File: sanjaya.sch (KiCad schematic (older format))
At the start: 10 parts, among them J1 PWR_SUPPLY, J15 Serial, J2 Digital_Input_Signals, J3 Digital_Gnd, J4 Screw_Terminal_01x03, J5 Screw_Terminal_01x03, J6 Screw_Terminal_01x02, J7 Screw_Terminal_01x02, U2 MCP9700T-ETT

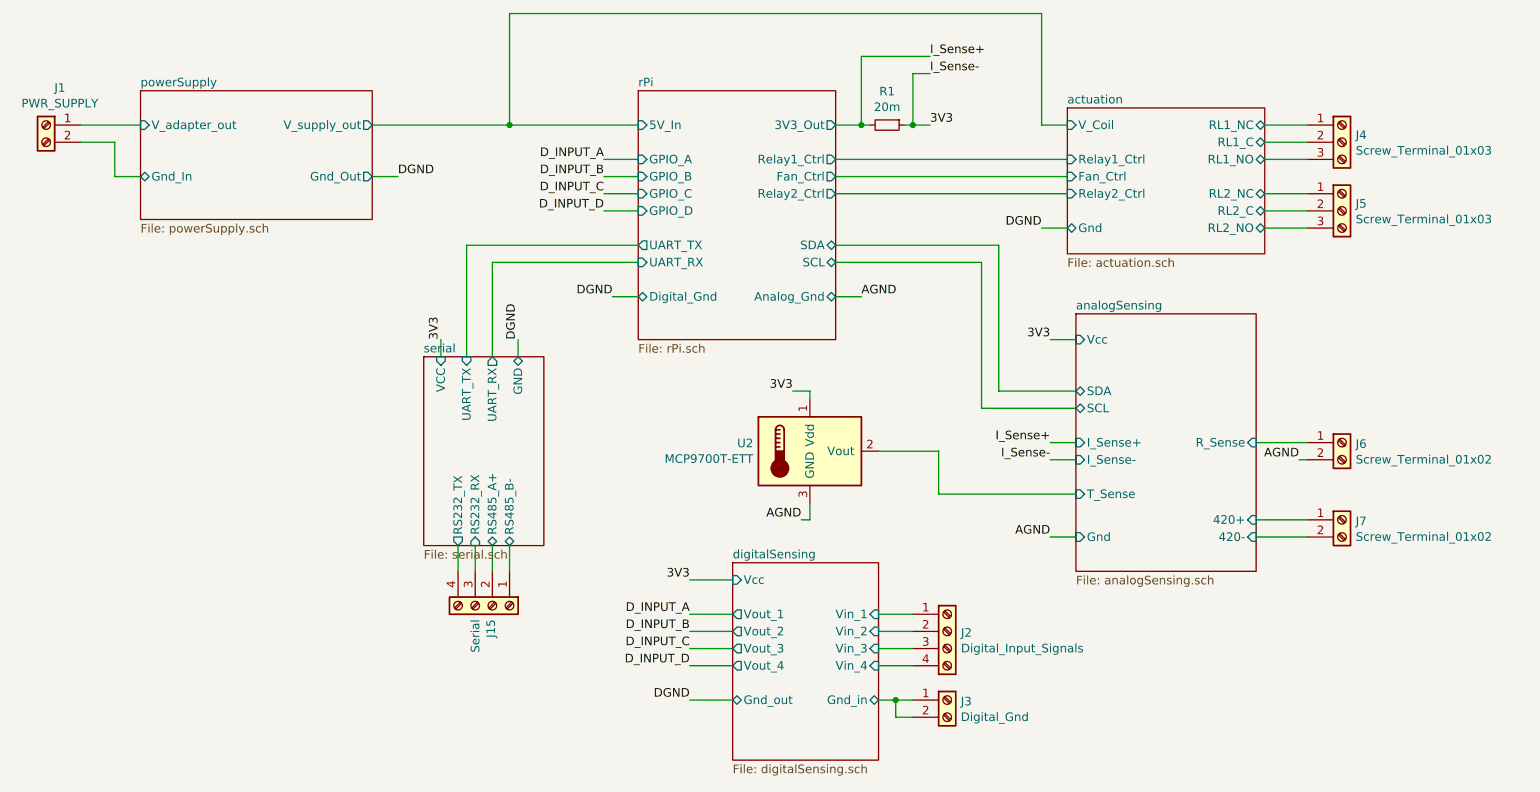
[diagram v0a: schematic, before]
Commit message: Changes: 1. Some net names, connector names changed to be more meaningful 2. I2C connector added 3. Mistake in power bank bypass connection rectified 4. Layout changed. Almost finalized.
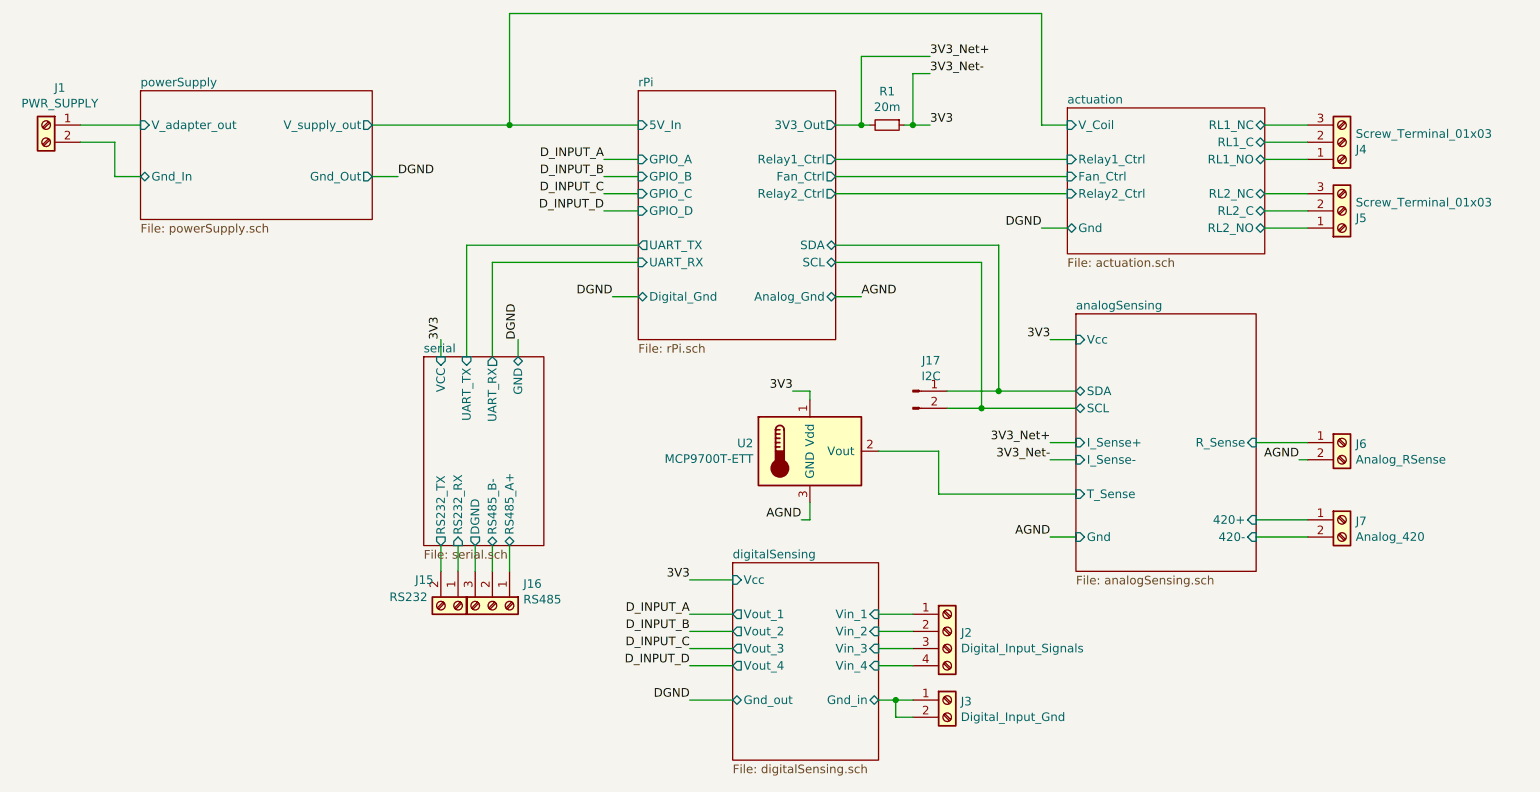
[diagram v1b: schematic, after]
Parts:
- removed J15: Serial, TerminalBlock_Phoenix:TerminalBlock_Phoenix_MKDS-1,5-4-5.08_1x04_P5.08mm_Horizontal, symbol Connector:Screw_Terminal_01x04
- added J15: RS232, TerminalBlock_Phoenix:TerminalBlock_Phoenix_MKDS-1,5-2-5.08_1x02_P5.08mm_Horizontal, symbol Connector:Screw_Terminal_01x02
- added J16: RS485, TerminalBlock_Phoenix:TerminalBlock_Phoenix_MKDS-1,5-3-5.08_1x03_P5.08mm_Horizontal, symbol Connector:Screw_Terminal_01x03
- added J17: I2C, Connector_JST:JST_EH_B02B-EH-A_1x02_P2.50mm_Vertical, symbol Connector:Conn_01x02_Male
- J3: value Digital_Gnd -> Digital_Input_Gnd
- J6: value Screw_Terminal_01x02 -> Analog_RSense
- J7: value Screw_Terminal_01x02 -> Analog_420
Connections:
- net actuation/RL1_NC: now also J4.3 (Pin_3); no longer J4.1 (Pin_1)
- net actuation/RL1_NO: now also J4.1 (Pin_1); no longer J4.3 (Pin_3)
- net actuation/RL2_NC: now also J5.3 (Pin_3); no longer J5.1 (Pin_1)
- net actuation/RL2_NO: now also J5.1 (Pin_1); no longer J5.3 (Pin_3)
- net analogSensing/SCL: now also J17.2 (Pin_2)
- net analogSensing/SDA: now also J17.1 (Pin_1)
- net serial/RS232_RX: now also J15.1 (Pin_1)
- net serial/RS232_TX: now also J15.2 (Pin_2)
- net serial/RS485_A+: now also J16.1 (Pin_1)
- net serial/RS485_B-: now also J16.2 (Pin_2)
- net I_Sense+ renamed 3V3_Net+
- new net serial/DGND: J16.3 (Pin_3)
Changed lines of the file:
@@
 Sheet 1 7
 Title "Sanjaya Gateway"
-Date "2018-10-02"
-Rev "0.6"
+Date "2018-10-05"
+Rev "0.7"
 Comp "Bodhileaf Technologies"
 Comment1 ""
@@
 F4 "GND" B T 4300 4000 50
 F5 "UART_RX" O T 4150 4000 50
-F6 "RS485_A+" B B 4150 5100 50
-F7 "RS485_B-" B B 4250 5100 50
-F8 "RS232_TX" O B 3950 5100 50
-F9 "RS232_RX" I B 4050 5100 50
+F6 "RS485_A+" B B 4250 5100 50
+F7 "RS485_B-" B B 4150 5100 50
+F8 "RS232_TX" O B 3850 5100 50
+F9 "RS232_RX" I B 3950 5100 50
+F10 "DGND" O B 4050 5100 50
 $EndSheet
 Text Label 4850 3650 2    50   ~ 0
@@
 	6150 2650 6300 2650
 Text Label 6700 2350 0    50   ~ 0
-I_Sense-
+3V3_Net-
 Text Label 6700 2250 0    50   ~ 0
-I_Sense+
+3V3_Net+
 Wire Wire Line
 	6300 2650 6300 2250
@@
 	3450 2650 4250 2650
 Text Label 7400 4500 2    50   ~ 0
-I_Sense+
+3V3_Net+
 Text Label 7400 4600 2    50   ~ 0
-I_Sense-
+3V3_Net-
 Wire Wire Line
 	7400 4500 7550 4500
@@
 P 6800 6000
 F 0 "J3" H 6879 5992 50  0000 L CNN
-F 1 "Digital_Gnd" H 6879 5901 50  0000 L CNN
+F 1 "Digital_Input_Gnd" H 6879 5901 50  0000 L CNN
 F 2 "TerminalBlock_Phoenix:TerminalBlock_Phoenix_MKDS-1,5-2-5.08_1x02_P5.08mm_Horizontal" H 6800 6000 50  0001 C CNN
 F 3 "~" H 6800 6000 50  0001 C CNN
@@
 P 9100 4500
 F 0 "J6" H 9180 4492 50  0000 L CNN
-F 1 "Screw_Terminal_01x02" H 9180 4401 50  0000 L CNN
+F 1 "Analog_RSense" H 9180 4401 50  0000 L CNN
 F 2 "TerminalBlock_Phoenix:TerminalBlock_Phoenix_MKDS-1,5-2-5.08_1x02_P5.08mm_Horizontal" H 9100 4500 50  0001 C CNN
 F 3 "~" H 9100 4500 50  0001 C CNN
@@
 P 9100 4950
 F 0 "J7" H 9180 4942 50  0000 L CNN
-F 1 "Screw_Terminal_01x02" H 9180 4851 50  0000 L CNN
+F 1 "Analog_420" H 9180 4851 50  0000 L CNN
 F 2 "TerminalBlock_Phoenix:TerminalBlock_Phoenix_MKDS-1,5-2-5.08_1x02_P5.08mm_Horizontal" H 9100 4950 50  0001 C CNN
 F 3 "~" H 9100 4950 50  0001 C CNN
@@
 F 3 "~" H 9100 2750 50  0001 C CNN
 	1    9100 2750
-	1    0    0    -1
+	1    0    0    1
 $EndComp
 $Comp
@@
 F 3 "~" H 9100 3150 50  0001 C CNN
 	1    9100 3150
-	1    0    0    -1
+	1    0    0    1
 $EndComp
 Wire Wire Line
@@
 Wire Wire Line
 	6750 4800 7550 4800
-$Comp
-L Connector:Screw_Terminal_01x04 J15
-U 1 1 5BB5228E
+Wire Wire Line
+	3950 5100 3950 5250
+Wire Wire Line
+	4050 5100 4050 5250
+Wire Wire Line
+	4150 5100 4150 5250
+Wire Wire Line
+	4250 5100 4250 5250
+Wire Wire Line
+	5000 3350 4000 3350
+Wire Wire Line
+	4000 3350 4000 4000
+Wire Wire Line
+	4150 4000 4150 3450
+Wire Wire Line
+	4150 3450 5000 3450
+$Comp
+L Connector:Screw_Terminal_01x03 J16
+U 1 1 5BB7BA6A
 P 4150 5450
-F 0 "J15" H 4230 5442 50  0000 L CNN
-F 1 "Serial" H 4230 5351 50  0000 L CNN
-F 2 "TerminalBlock_Phoenix:TerminalBlock_Phoenix_MKDS-1,5-4-5.08_1x04_P5.08mm_Horizontal" H 4150 5450 50  0001 C CNN
+F 0 "J16" V 4023 5630 50  0000 L CNN
+F 1 "RS485" V 4114 5630 50  0000 L CNN
+F 2 "TerminalBlock_Phoenix:TerminalBlock_Phoenix_MKDS-1,5-3-5.08_1x03_P5.08mm_Horizontal" H 4150 5450 50  0001 C CNN
 F 3 "~" H 4150 5450 50  0001 C CNN
 	1    4150 5450
 	0    1    1    0
 $EndComp
-Wire Wire Line
-	3950 5100 3950 5250
-Wire Wire Line
-	4050 5100 4050 5250
-Wire Wire Line
-	4150 5100 4150 5250
-Wire Wire Line
-	4250 5100 4250 5250
-Wire Wire Line
-	5000 3350 4000 3350
-Wire Wire Line
-	4000 3350 4000 4000
-Wire Wire Line
-	4150 4000 4150 3450
-Wire Wire Line
-	4150 3450 5000 3450
+$Comp
+L Connector:Screw_Terminal_01x02 J15
+U 1 1 5BB7BBDA
+P 3950 5450
+F 0 "J15" V 3800 5200 50  0000 L CNN
+F 1 "RS232" V 3900 5050 50  0000 L CNN
+F 2 "TerminalBlock_Phoenix:TerminalBlock_Phoenix_MKDS-1,5-2-5.08_1x02_P5.08mm_Horizontal" H 3950 5450 50  0001 C CNN
+F 3 "~" H 3950 5450 50  0001 C CNN
+	1    3950 5450
+	0    1    1    0
+$EndComp
+Wire Wire Line
+	3850 5250 3850 5100
+$Comp
+L Connector:Conn_01x02_Male J17
+U 1 1 5BB7EB2C
+P 6600 4200
+F 0 "J17" H 6706 4378 50  0000 C CNN
+F 1 "I2C" H 6706 4287 50  0000 C CNN
+F 2 "Connector_JST:JST_EH_B02B-EH-A_1x02_P2.50mm_Vertical" H 6600 4200 50  0001 C CNN
+F 3 "~" H 6600 4200 50  0001 C CNN
+	1    6600 4200
+	1    0    0    -1
+$EndComp
+Wire Wire Line
+	6800 4200 7100 4200
+Connection ~ 7100 4200
+Wire Wire Line
+	6800 4300 7000 4300
+Connection ~ 7000 4300
 $EndSCHEMATC

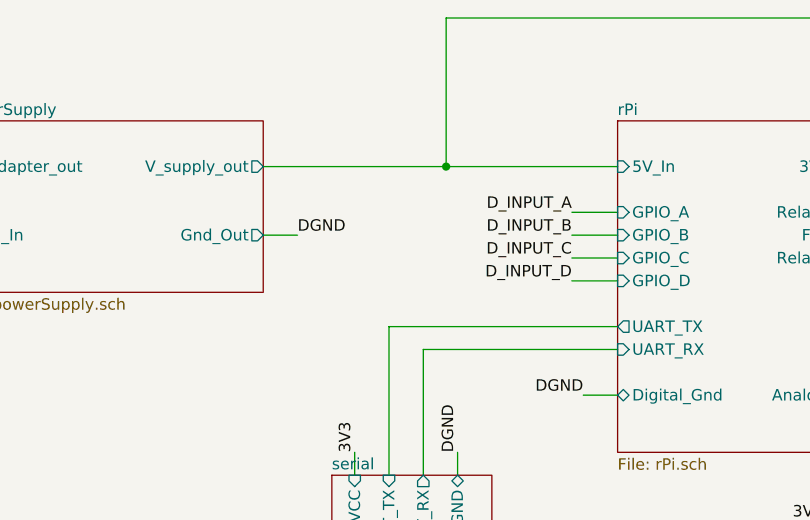
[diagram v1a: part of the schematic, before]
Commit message: Changes: 1. Added a power LED 2. Added PPTC to the inputs of optocoupler 3. Added PPTC to the transceiver side of the RS232 driver 4. Corrected ADC footprint
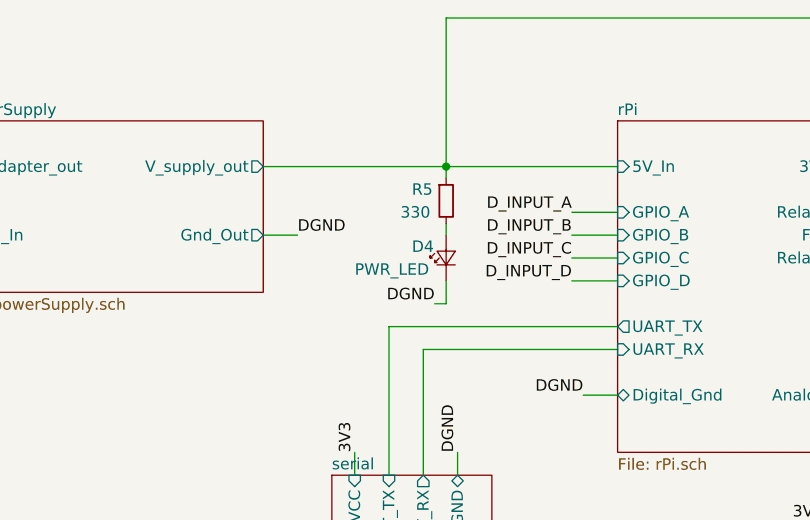
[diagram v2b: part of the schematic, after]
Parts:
- added D4: PWR_LED, LED_SMD:LED_0805_2012Metric, symbol Device:LED_Small
- added R5: 330, Resistor_SMD:R_0805_2012Metric, symbol Device:R_Small
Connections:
- net DGND: now also D4.1 (K)
- net actuation/V_Coil: now also R5.1
- new net: D4.2 (A), R5.2
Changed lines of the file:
@@
 	6800 4300 7000 4300
 Connection ~ 7000 4300
+$Comp
+L Device:R_Small R5
+U 1 1 5BBFB659
+P 4250 2800
+F 0 "R5" H 4100 2850 50  0000 L CNN
+F 1 "330" H 4050 2750 50  0000 L CNN
+F 2 "Resistor_SMD:R_0805_2012Metric" H 4250 2800 50  0001 C CNN
+F 3 "~" H 4250 2800 50  0001 C CNN
+	1    4250 2800
+	1    0    0    -1
+$EndComp
+$Comp
+L Device:LED_Small D4
+U 1 1 5BBFB89A
+P 4250 3050
+F 0 "D4" V 4300 3200 50  0000 R CNN
+F 1 "PWR_LED" V 4200 3450 50  0000 R CNN
+F 2 "LED_SMD:LED_0805_2012Metric" V 4250 3050 50  0001 C CNN
+F 3 "~" V 4250 3050 50  0001 C CNN
+	1    4250 3050
+	0    -1   -1   0
+$EndComp
+Wire Wire Line
+	4250 2650 4250 2700
+Wire Wire Line
+	4250 2900 4250 2950
+Text Label 4200 3250 2    50   ~ 0
+DGND
+Wire Wire Line
+	4250 3150 4250 3250
+Wire Wire Line
+	4250 3250 4200 3250
 $EndSCHEMATC

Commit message: Screw connectors footprint changed to 2.54mm ones and relayout done for all terminal blocks
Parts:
- J1, J15, J3, J6, J7: footprint TerminalBlock_Phoenix:TerminalBlock_Phoenix_MKDS-1,5-2-5.08_1x02_P5.08mm_Horizontal -> TerminalBlock_Phoenix:TerminalBlock_Phoenix_MPT-0,5-2-2.54_1x02_P2.54mm_Horizontal
- J16, J4, J5: footprint TerminalBlock_Phoenix:TerminalBlock_Phoenix_MKDS-1,5-3-5.08_1x03_P5.08mm_Horizontal -> TerminalBlock_Phoenix:TerminalBlock_Phoenix_MPT-0,5-3-2.54_1x03_P2.54mm_Horizontal
- J2: footprint TerminalBlock_Phoenix:TerminalBlock_Phoenix_MKDS-1,5-4-5.08_1x04_P5.08mm_Horizontal -> TerminalBlock_Phoenix:TerminalBlock_Phoenix_MPT-0,5-4-2.54_1x04_P2.54mm_Horizontal
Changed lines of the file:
@@
 F 0 "J1" H 1470 2867 50  0000 C CNN
 F 1 "PWR_SUPPLY" H 1470 2776 50  0000 C CNN
-F 2 "TerminalBlock_Phoenix:TerminalBlock_Phoenix_MKDS-1,5-2-5.08_1x02_P5.08mm_Horizontal" H 1550 2650 50  0001 C CNN
+F 2 "TerminalBlock_Phoenix:TerminalBlock_Phoenix_MPT-0,5-2-2.54_1x02_P2.54mm_Horizontal" H 1550 2650 50  0001 C CNN
 F 3 "~" H 1550 2650 50  0001 C CNN
 	1    1550 2650
@@
 F 0 "J2" H 6880 5592 50  0000 L CNN
 F 1 "Digital_Input_Signals" H 6880 5501 50  0000 L CNN
-F 2 "TerminalBlock_Phoenix:TerminalBlock_Phoenix_MKDS-1,5-4-5.08_1x04_P5.08mm_Horizontal" H 6800 5600 50  0001 C CNN
+F 2 "TerminalBlock_Phoenix:TerminalBlock_Phoenix_MPT-0,5-4-2.54_1x04_P2.54mm_Horizontal" H 6800 5600 50  0001 C CNN
 F 3 "~" H 6800 5600 50  0001 C CNN
 	1    6800 5600
@@
 F 0 "J3" H 6879 5992 50  0000 L CNN
 F 1 "Digital_Input_Gnd" H 6879 5901 50  0000 L CNN
-F 2 "TerminalBlock_Phoenix:TerminalBlock_Phoenix_MKDS-1,5-2-5.08_1x02_P5.08mm_Horizontal" H 6800 6000 50  0001 C CNN
+F 2 "TerminalBlock_Phoenix:TerminalBlock_Phoenix_MPT-0,5-2-2.54_1x02_P2.54mm_Horizontal" H 6800 6000 50  0001 C CNN
 F 3 "~" H 6800 6000 50  0001 C CNN
 	1    6800 6000
@@
 F 0 "J6" H 9180 4492 50  0000 L CNN
 F 1 "Analog_RSense" H 9180 4401 50  0000 L CNN
-F 2 "TerminalBlock_Phoenix:TerminalBlock_Phoenix_MKDS-1,5-2-5.08_1x02_P5.08mm_Horizontal" H 9100 4500 50  0001 C CNN
+F 2 "TerminalBlock_Phoenix:TerminalBlock_Phoenix_MPT-0,5-2-2.54_1x02_P2.54mm_Horizontal" H 9100 4500 50  0001 C CNN
 F 3 "~" H 9100 4500 50  0001 C CNN
 	1    9100 4500
@@
 F 0 "J7" H 9180 4942 50  0000 L CNN
 F 1 "Analog_420" H 9180 4851 50  0000 L CNN
-F 2 "TerminalBlock_Phoenix:TerminalBlock_Phoenix_MKDS-1,5-2-5.08_1x02_P5.08mm_Horizontal" H 9100 4950 50  0001 C CNN
+F 2 "TerminalBlock_Phoenix:TerminalBlock_Phoenix_MPT-0,5-2-2.54_1x02_P2.54mm_Horizontal" H 9100 4950 50  0001 C CNN
 F 3 "~" H 9100 4950 50  0001 C CNN
 	1    9100 4950
@@
 F 0 "J4" H 9180 2792 50  0000 L CNN
 F 1 "Screw_Terminal_01x03" H 9180 2701 50  0000 L CNN
-F 2 "TerminalBlock_Phoenix:TerminalBlock_Phoenix_MKDS-1,5-3-5.08_1x03_P5.08mm_Horizontal" H 9100 2750 50  0001 C CNN
+F 2 "TerminalBlock_Phoenix:TerminalBlock_Phoenix_MPT-0,5-3-2.54_1x03_P2.54mm_Horizontal" H 9100 2750 50  0001 C CNN
 F 3 "~" H 9100 2750 50  0001 C CNN
 	1    9100 2750
@@
 F 0 "J5" H 9180 3192 50  0000 L CNN
 F 1 "Screw_Terminal_01x03" H 9180 3101 50  0000 L CNN
-F 2 "TerminalBlock_Phoenix:TerminalBlock_Phoenix_MKDS-1,5-3-5.08_1x03_P5.08mm_Horizontal" H 9100 3150 50  0001 C CNN
+F 2 "TerminalBlock_Phoenix:TerminalBlock_Phoenix_MPT-0,5-3-2.54_1x03_P2.54mm_Horizontal" H 9100 3150 50  0001 C CNN
 F 3 "~" H 9100 3150 50  0001 C CNN
 	1    9100 3150
@@
 F 0 "J16" V 4023 5630 50  0000 L CNN
 F 1 "RS485" V 4114 5630 50  0000 L CNN
-F 2 "TerminalBlock_Phoenix:TerminalBlock_Phoenix_MKDS-1,5-3-5.08_1x03_P5.08mm_Horizontal" H 4150 5450 50  0001 C CNN
+F 2 "TerminalBlock_Phoenix:TerminalBlock_Phoenix_MPT-0,5-3-2.54_1x03_P2.54mm_Horizontal" H 4150 5450 50  0001 C CNN
 F 3 "~" H 4150 5450 50  0001 C CNN
 	1    4150 5450
@@
 F 0 "J15" V 3800 5200 50  0000 L CNN
 F 1 "RS232" V 3900 5050 50  0000 L CNN
-F 2 "TerminalBlock_Phoenix:TerminalBlock_Phoenix_MKDS-1,5-2-5.08_1x02_P5.08mm_Horizontal" H 3950 5450 50  0001 C CNN
+F 2 "TerminalBlock_Phoenix:TerminalBlock_Phoenix_MPT-0,5-2-2.54_1x02_P2.54mm_Horizontal" H 3950 5450 50  0001 C CNN
 F 3 "~" H 3950 5450 50  0001 C CNN
 	1    3950 5450
